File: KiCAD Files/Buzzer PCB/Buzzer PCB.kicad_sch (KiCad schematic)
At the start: 12 parts, among them J1 JST-PH Battery IN, J2 JST-PH Feather BAT OUT, J3 Comidox Boost Module, J4 Feather D13, Q1 S8050, SW1 SS12D00G5

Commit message: FlatCAM ready
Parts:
- removed J3: Comidox Boost Module, Connector_PinHeader_2.54mm:PinHeader_1x03_P2.54mm_Vertical, symbol Connector:Conn_01x03_Pin
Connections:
- net BOOST_5V is gone; now on net SW_BAT: BZ1.1 (+), C1.1, C2.1, D1.1 (K)
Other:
- note added: "Flyback diode: cathode/stripe to SW_BAT, anode to BUZZER_LOW"
- note removed: "Boost module pin order per markdown: VIN, GND, VOUT"
- note removed: "Flyback diode: cathode/stripe to BOOST_5V, anode to BUZZER_LOW"
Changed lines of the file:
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@@
-	)
-	(symbol
-		(lib_id "Connector:Conn_01x03_Pin")
-		(at 25.4 68.58 0)
-		(unit 1)
-		(exclude_from_sim no)
-		(in_bom yes)
-		(on_board yes)
-		(dnp no)
-		(property "Reference" "J3"
-			(at 25.4 63.5 0)
-			(effects (font (size 1.27 1.27)))
-		)
-		(property "Value" "Comidox Boost Module"
-			(at 25.4 73.66 0)
-			(effects (font (size 1.27 1.27)))
-		)
-		(property "Footprint" "Connector_PinHeader_2.54mm:PinHeader_1x03_P2.54mm_Vertical"
-			(at 25.4 68.58 0)
-			(hide yes)
-			(effects (font (size 1.27 1.27)))
-		)
-		(property "Datasheet" ""
-			(at 25.4 68.58 0)
-			(hide yes)
-			(effects (font (size 1.27 1.27)))
-		)
-		(pin "1")
-		(pin "2")
-		(pin "3")
-		(instances (project "Buzzer PCB" (path "/6e2f3a7a-f7cb-4ca1-a616-e9fb51cc60ce" (reference "J3") (unit 1))))
-	)
-	(label "SW_BAT"
-		(at 30.48 66.04 0)
-		(effects (font (size 1.27 1.27)))
-	)
-	(label "GND"
-		(at 30.48 68.58 0)
-		(effects (font (size 1.27 1.27)))
-	)
-	(label "BOOST_5V"
-		(at 30.48 71.12 0)
-		(effects (font (size 1.27 1.27)))
-	)
-	(text "Boost module pin order per markdown: VIN, GND, VOUT"
-		(at 15.24 78.74 0)
-		(effects (font (size 1.1 1.1)) (justify left bottom))
 	)
 	(symbol
@@
 		(instances (project "Buzzer PCB" (path "/6e2f3a7a-f7cb-4ca1-a616-e9fb51cc60ce" (reference "BZ1") (unit 1))))
 	)
-	(label "BOOST_5V"
+	(label "SW_BAT"
 		(at 114.3 86.36 0)
 		(effects (font (size 1.27 1.27)))
@@
 		(instances (project "Buzzer PCB" (path "/6e2f3a7a-f7cb-4ca1-a616-e9fb51cc60ce" (reference "D1") (unit 1))))
 	)
-	(label "BOOST_5V"
+	(label "SW_BAT"
 		(at 113.03 99.06 0)
 		(effects (font (size 1.27 1.27)))
@@
 		(effects (font (size 1.27 1.27)))
 	)
-	(text "Flyback diode: cathode/stripe to BOOST_5V, anode to BUZZER_LOW"
+	(text "Flyback diode: cathode/stripe to SW_BAT, anode to BUZZER_LOW"
 		(at 99.06 106.68 0)
 		(effects (font (size 1.1 1.1)) (justify left bottom))
@@
 		(instances (project "Buzzer PCB" (path "/6e2f3a7a-f7cb-4ca1-a616-e9fb51cc60ce" (reference "C1") (unit 1))))
 	)
-	(label "BOOST_5V"
+	(label "SW_BAT"
 		(at 142.24 85.09 0)
 		(effects (font (size 1.27 1.27)))
@@
 		(instances (project "Buzzer PCB" (path "/6e2f3a7a-f7cb-4ca1-a616-e9fb51cc60ce" (reference "C2") (unit 1))))
 	)
-	(label "BOOST_5V"
+	(label "SW_BAT"
 		(at 154.94 85.09 0)
 		(effects (font (size 1.27 1.27)))

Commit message: V2 PCB done
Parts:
- C1: value 47-100uF -> 47-100uF electrolytic
- C2: value 0.1uF -> 0.1uF ceramic
- J1, J2: footprint Connector_JST:JST_PH_S2B-PH-K_1x02_P2.00mm_Horizontal -> Connector_JST:JST_PH_B2B-PH-K_1x02_P2.00mm_Vertical
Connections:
- net BAT_IN: now also J1.2 (Pin_2); no longer J1.1 (Pin_1)
- net GND: now also J1.1 (Pin_1), J2.1 (Pin_1); no longer J1.2 (Pin_2), J2.2 (Pin_2)
- net SW_BAT: now also J2.2 (Pin_2); no longer J2.1 (Pin_1)
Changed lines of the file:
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@@
 			(effects (font (size 1.27 1.27)))
 		)
-		(property "Footprint" "Connector_JST:JST_PH_S2B-PH-K_1x02_P2.00mm_Horizontal"
+		(property "Footprint" "Connector_JST:JST_PH_B2B-PH-K_1x02_P2.00mm_Vertical"
 			(at 25.4 40.64 0)
 			(hide yes)
@@
 		(instances (project "Buzzer PCB" (path "/6e2f3a7a-f7cb-4ca1-a616-e9fb51cc60ce" (reference "J1") (unit 1))))
 	)
+	(label "GND"
+		(at 30.48 40.64 0)
+		(effects (font (size 1.27 1.27)))
+	)
 	(label "BAT_IN"
-		(at 30.48 40.64 0)
-		(effects (font (size 1.27 1.27)))
-	)
-	(label "GND"
 		(at 30.48 43.18 0)
 		(effects (font (size 1.27 1.27)))
@@
 			(effects (font (size 1.27 1.27)))
 		)
-		(property "Footprint" "Connector_JST:JST_PH_S2B-PH-K_1x02_P2.00mm_Horizontal"
+		(property "Footprint" "Connector_JST:JST_PH_B2B-PH-K_1x02_P2.00mm_Vertical"
 			(at 76.2 40.64 0)
 			(hide yes)
@@
 		(instances (project "Buzzer PCB" (path "/6e2f3a7a-f7cb-4ca1-a616-e9fb51cc60ce" (reference "J2") (unit 1))))
 	)
-	(label "SW_BAT"
+	(label "GND"
 		(at 81.28 40.64 0)
 		(effects (font (size 1.27 1.27)))
 	)
-	(label "GND"
+	(label "SW_BAT"
 		(at 81.28 43.18 0)
 		(effects (font (size 1.27 1.27)))
@@
 			(effects (font (size 1.27 1.27)))
 		)
-		(property "Value" "47-100uF"
+		(property "Value" "47-100uF electrolytic"
 			(at 142.24 93.98 0)
 			(effects (font (size 1.27 1.27)))
@@
 			(effects (font (size 1.27 1.27)))
 		)
-		(property "Value" "0.1uF"
+		(property "Value" "0.1uF ceramic"
 			(at 154.94 93.98 0)
 			(effects (font (size 1.27 1.27)))

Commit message: two_sided
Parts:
- J1, J2: footprint Connector_JST:JST_PH_B2B-PH-K_1x02_P2.00mm_Vertical -> Connector_JST:JST_PH_S2B-PH-K_1x02_P2.00mm_Horizontal
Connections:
- net BAT_IN: now also J1.1 (Pin_1); no longer J1.2 (Pin_2)
- net GND: now also J1.2 (Pin_2), J2.2 (Pin_2); no longer J1.1 (Pin_1), J2.1 (Pin_1)
- net SW_BAT: now also J2.1 (Pin_1); no longer J2.2 (Pin_2)
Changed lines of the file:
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@@
 			(effects (font (size 1.27 1.27)))
 		)
-		(property "Footprint" "Connector_JST:JST_PH_B2B-PH-K_1x02_P2.00mm_Vertical"
+		(property "Footprint" "Connector_JST:JST_PH_S2B-PH-K_1x02_P2.00mm_Horizontal"
 			(at 25.4 40.64 0)
 			(hide yes)
@@
 		(instances (project "Buzzer PCB" (path "/6e2f3a7a-f7cb-4ca1-a616-e9fb51cc60ce" (reference "J1") (unit 1))))
 	)
-	(label "GND"
+	(label "BAT_IN"
 		(at 30.48 40.64 0)
 		(effects (font (size 1.27 1.27)))
 	)
-	(label "BAT_IN"
+	(label "GND"
 		(at 30.48 43.18 0)
 		(effects (font (size 1.27 1.27)))
@@
 			(effects (font (size 1.27 1.27)))
 		)
-		(property "Footprint" "Connector_JST:JST_PH_B2B-PH-K_1x02_P2.00mm_Vertical"
+		(property "Footprint" "Connector_JST:JST_PH_S2B-PH-K_1x02_P2.00mm_Horizontal"
 			(at 76.2 40.64 0)
 			(hide yes)
@@
 		(instances (project "Buzzer PCB" (path "/6e2f3a7a-f7cb-4ca1-a616-e9fb51cc60ce" (reference "J2") (unit 1))))
 	)
-	(label "GND"
+	(label "SW_BAT"
 		(at 81.28 40.64 0)
 		(effects (font (size 1.27 1.27)))
 	)
-	(label "SW_BAT"
+	(label "GND"
 		(at 81.28 43.18 0)
 		(effects (font (size 1.27 1.27)))

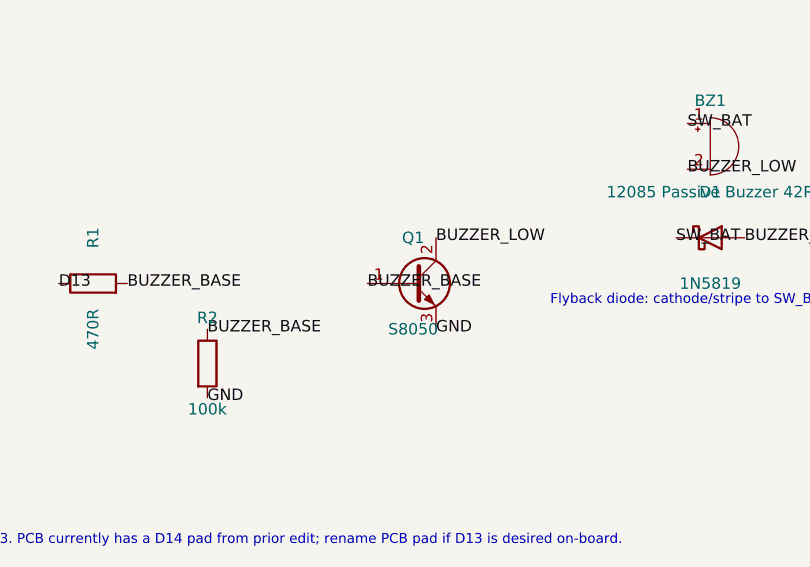
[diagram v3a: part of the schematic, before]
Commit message: Fix S8050 pinout and buzzer test interval
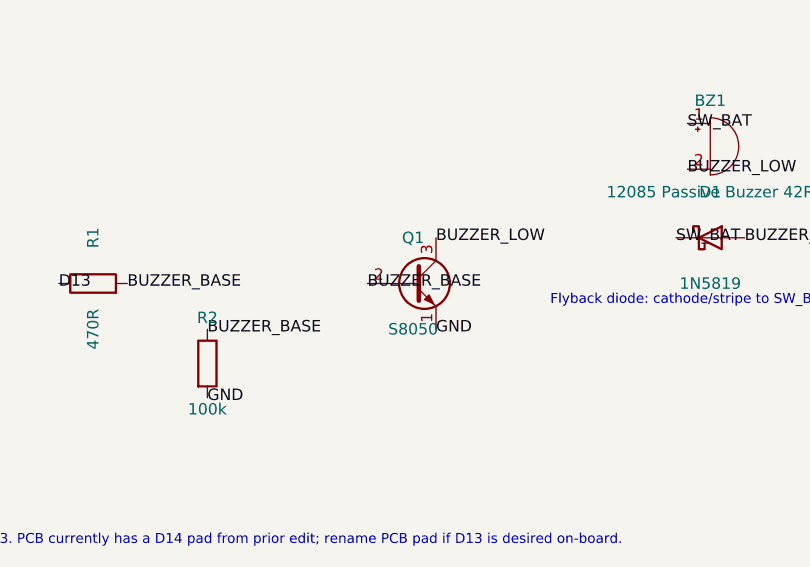
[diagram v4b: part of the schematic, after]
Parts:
- Q1: symbol Transistor_BJT:Q_NPN_BCE -> Transistor_BJT:Q_NPN_EBC
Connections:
- net BUZZER_BASE: now also Q1.2 (B); no longer Q1.1 (B)
- net BUZZER_LOW: now also Q1.3 (C); no longer Q1.2 (C)
- net GND: now also Q1.1 (E); no longer Q1.3 (E)
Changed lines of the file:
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@@
 	)
 	(symbol
-		(lib_id "Transistor_BJT:Q_NPN_BCE")
+		(lib_id "Transistor_BJT:Q_NPN_EBC")
 		(at 83.82 104.14 0)
 		(unit 1)
